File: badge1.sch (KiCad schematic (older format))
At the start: 21 parts, among them P1 CONN_01X04, P2 USB_A, P3 CONN_01X04, SW1 SW_PUSH, U1 badge_hole, U2 custom_logo, U3 Hillhacks_logo, U4 proto_area

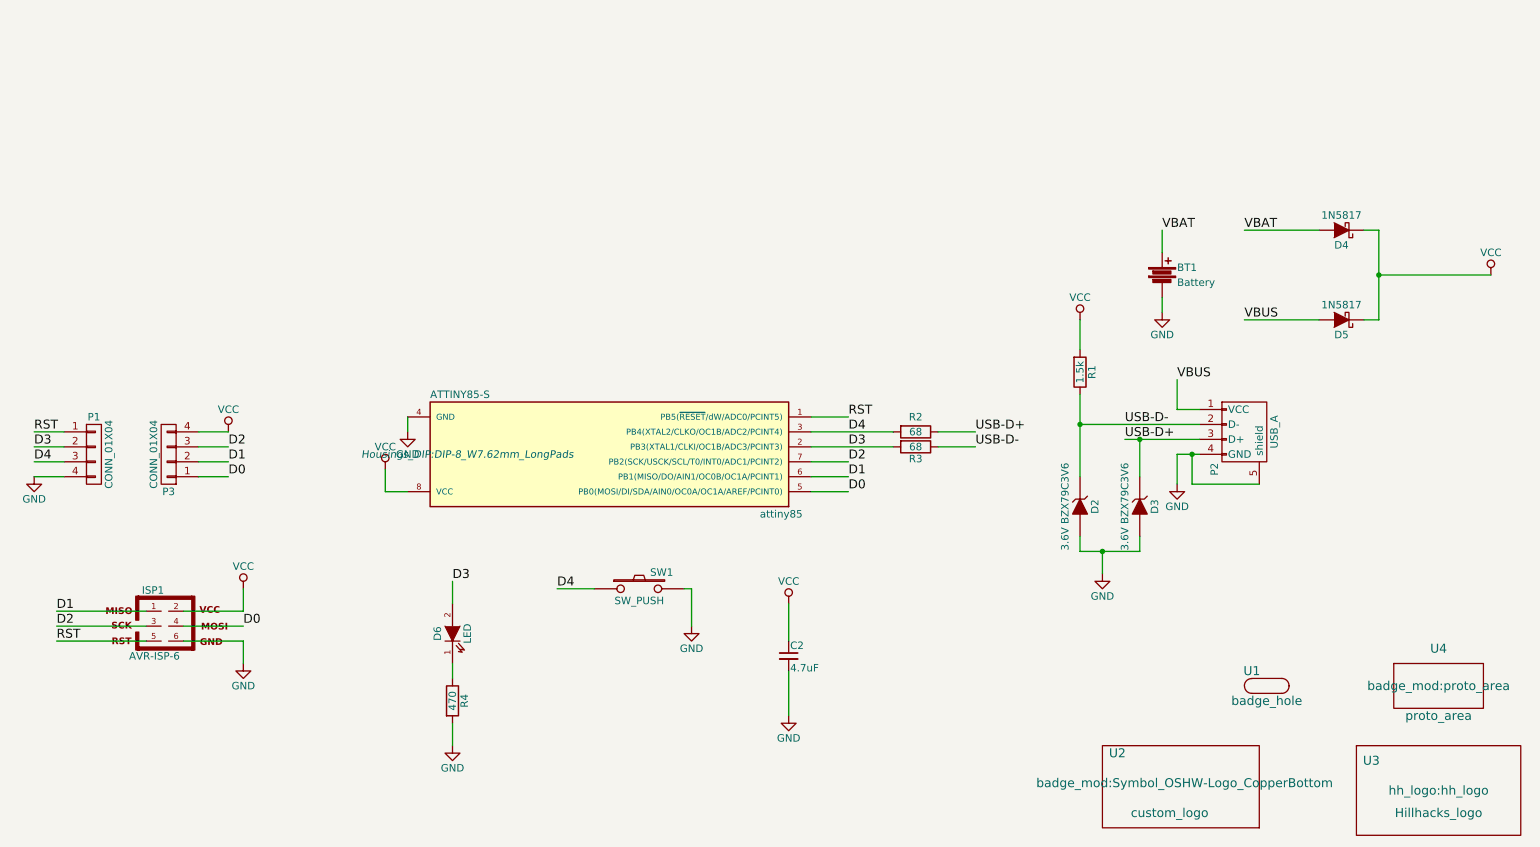
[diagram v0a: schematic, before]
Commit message: Updated with @anool's comments.
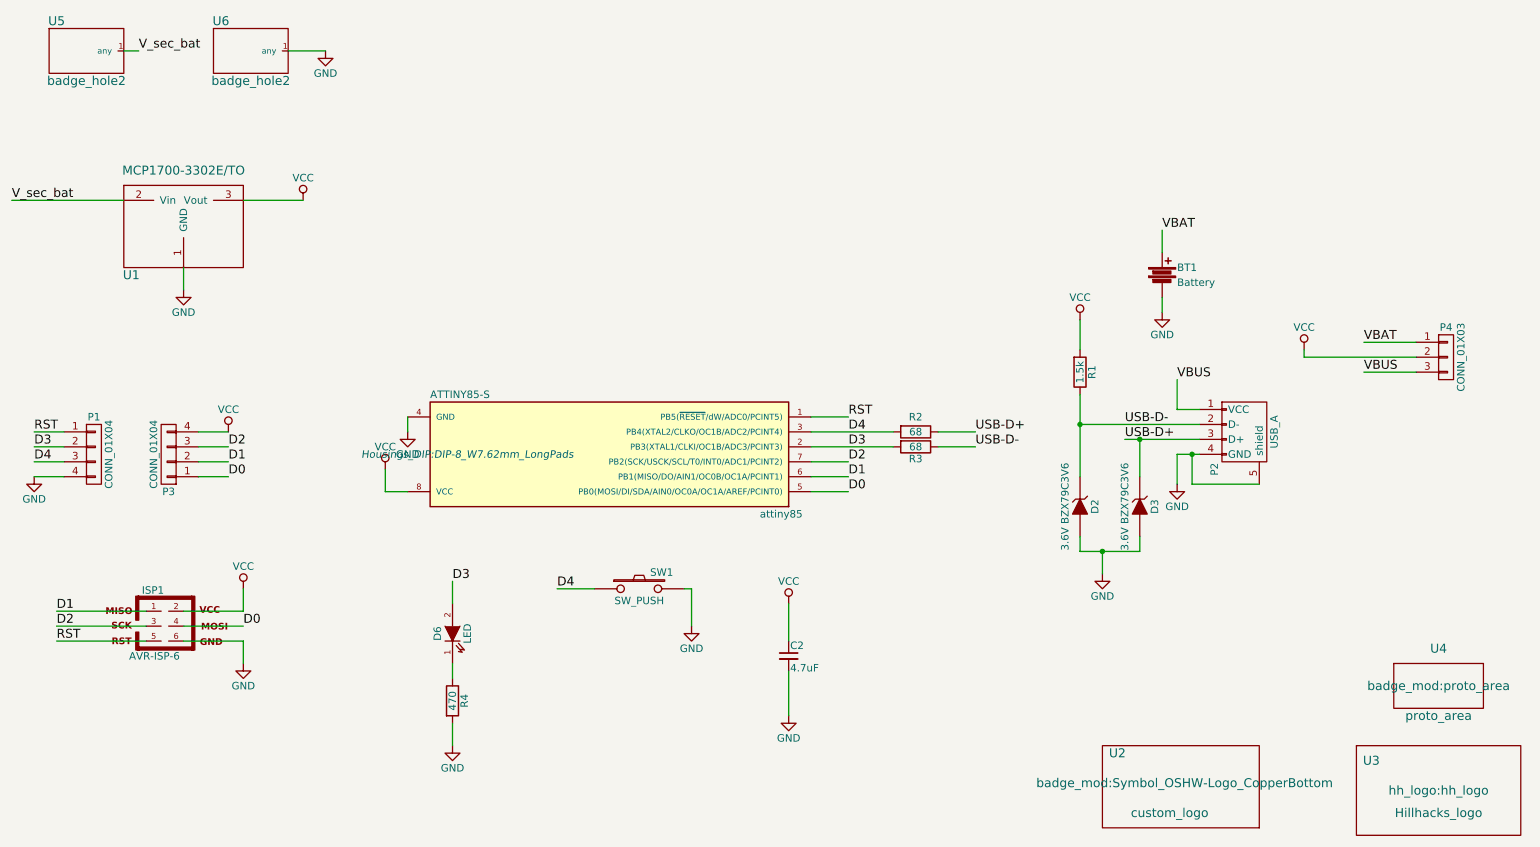
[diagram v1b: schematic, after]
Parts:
- removed D4, D5: 1N5817, Diodes_ThroughHole:Diode_DO-41_SOD81_Horizontal_RM10, symbol D_Schottky
- removed U1: badge_hole, badge_mod:badge_hole_6mmx3mm, symbol badge_hole
- added P4: CONN_01X03, Pin_Headers:Pin_Header_Straight_1x03, symbol CONN_01X03
- added U1: MCP1700-3302E/TO, TO_SOT_Packages_THT:TO-92_Molded_Narrow, symbol MCP1700-3302E/TO
- added U5, U6: badge_hole2, badge_mod:badge_hole_6mmx3mm(+2mmCu), symbol badge_hole2
- R1, R2, R3, R4: footprint Resistors_ThroughHole:Resistor_Vertical_RM5mm -> Resistors_ThroughHole:Resistor_Horizontal_RM10mm
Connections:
- net GND: now also U1.1 (GND), U6.1 (any)
- net VBAT: now also P4.1 (P1)
- net VBUS: now also P4.3 (P3)
- net VCC: now also P4.2 (P2), U1.3 (Vout)
- new net V_sec_bat: U1.2 (Vin), U5.1 (any)
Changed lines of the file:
@@
 RST
 $Comp
-L VCC #PWR01
+L VCC #PWR8
 U 1 1 56D1C9E6
 P 3350 3850
-F 0 "#PWR01" H 3350 3700 50  0001 C CNN
+F 0 "#PWR8" H 3350 3700 50  0001 C CNN
 F 1 "VCC" H 3350 4000 50  0000 C CNN
 F 2 "" H 3350 3850 50  0000 C CNN
@@
 $EndComp
 $Comp
-L GND #PWR02
+L GND #PWR9
 U 1 1 56D1CA06
 P 3500 3600
-F 0 "#PWR02" H 3500 3350 50  0001 C CNN
+F 0 "#PWR9" H 3500 3350 50  0001 C CNN
 F 1 "GND" H 3500 3450 50  0000 C CNN
 F 2 "" H 3500 3600 50  0000 C CNN
@@
 D0
 $Comp
-L GND #PWR03
+L GND #PWR17
 U 1 1 56D1CAE6
 P 8650 3950
-F 0 "#PWR03" H 8650 3700 50  0001 C CNN
+F 0 "#PWR17" H 8650 3700 50  0001 C CNN
 F 1 "GND" H 8650 3800 50  0000 C CNN
 F 2 "" H 8650 3950 50  0000 C CNN
@@
 F 0 "R3" V 6980 3700 50  0000 C CNN
 F 1 "68" V 6900 3700 50  0000 C CNN
-F 2 "Resistors_ThroughHole:Resistor_Vertical_RM5mm" V 6830 3700 50  0001 C CNN
+F 2 "Resistors_ThroughHole:Resistor_Horizontal_RM10mm" V 6830 3700 50  0001 C CNN
 F 3 "" H 6900 3700 50  0000 C CNN
 F 4 "311-68GRCT-ND" V 6900 3700 60  0001 C CNN "digikey"
@@
 F 0 "R2" V 6800 3600 50  0000 C CNN
 F 1 "68" V 6900 3600 50  0000 C CNN
-F 2 "Resistors_ThroughHole:Resistor_Vertical_RM5mm" V 6830 3600 50  0001 C CNN
+F 2 "Resistors_ThroughHole:Resistor_Horizontal_RM10mm" V 6830 3600 50  0001 C CNN
 F 3 "" H 6900 3600 50  0000 C CNN
 	1    6900 3600
@@
 $EndComp
 $Comp
-L GND #PWR04
+L GND #PWR15
 U 1 1 56D1CE23
 P 8150 4550
-F 0 "#PWR04" H 8150 4300 50  0001 C CNN
+F 0 "#PWR15" H 8150 4300 50  0001 C CNN
 F 1 "GND" H 8150 4400 50  0000 C CNN
 F 2 "" H 8150 4550 50  0000 C CNN
@@
 D0
 $Comp
-L GND #PWR05
+L GND #PWR5
 U 1 1 56D1D00C
 P 2400 5150
-F 0 "#PWR05" H 2400 4900 50  0001 C CNN
+F 0 "#PWR5" H 2400 4900 50  0001 C CNN
 F 1 "GND" H 2400 5000 50  0000 C CNN
 F 2 "" H 2400 5150 50  0000 C CNN
@@
 $EndComp
 $Comp
-L VCC #PWR06
+L VCC #PWR4
 U 1 1 56D1D050
 P 2400 4650
-F 0 "#PWR06" H 2400 4500 50  0001 C CNN
+F 0 "#PWR4" H 2400 4500 50  0001 C CNN
 F 1 "VCC" H 2400 4800 50  0000 C CNN
 F 2 "" H 2400 4650 50  0000 C CNN
@@
 $EndComp
 $Comp
-L GND #PWR07
+L GND #PWR13
 U 1 1 56D1D3A0
 P 6050 5500
-F 0 "#PWR07" H 6050 5250 50  0001 C CNN
+F 0 "#PWR13" H 6050 5250 50  0001 C CNN
 F 1 "GND" H 6050 5350 50  0000 C CNN
 F 2 "" H 6050 5500 50  0000 C CNN
@@
 $EndComp
 $Comp
-L VCC #PWR08
+L VCC #PWR12
 U 1 1 56D1D3F8
 P 6050 4750
-F 0 "#PWR08" H 6050 4600 50  0001 C CNN
+F 0 "#PWR12" H 6050 4600 50  0001 C CNN
 F 1 "VCC" H 6050 4900 50  0000 C CNN
 F 2 "" H 6050 4750 50  0000 C CNN
@@
 $EndComp
 $Comp
-L GND #PWR09
+L GND #PWR16
 U 1 1 56D1FCE5
 P 8550 2800
-F 0 "#PWR09" H 8550 2550 50  0001 C CNN
+F 0 "#PWR16" H 8550 2550 50  0001 C CNN
 F 1 "GND" H 8550 2650 50  0000 C CNN
 F 2 "" H 8550 2800 50  0000 C CNN
@@
 	0    1    1    0
 $EndComp
-$Comp
-L badge_hole U1
-U 1 1 56D21275
-P 9250 5300
-F 0 "U1" H 9150 5400 60  0000 C CNN
-F 1 "badge_hole" H 9250 5200 60  0000 C CNN
-F 2 "badge_mod:badge_hole_6mmx3mm" H 9250 5350 60  0001 C CNN
-F 3 "" H 9250 5350 60  0000 C CNN
-	1    9250 5300
-	1    0    0    -1
-$EndComp
 Text Label 8550 2250 0    60   ~ 0
 VBAT
 Text Label 8650 3250 0    60   ~ 0
 VBUS
-Text Label 9100 2250 0    60   ~ 0
+Text Label 9900 3000 0    60   ~ 0
 VBAT
-Text Label 9100 2850 0    60   ~ 0
+Text Label 9900 3200 0    60   ~ 0
 VBUS
 $Comp
@@
 $EndComp
 $Comp
-L GND #PWR010
+L GND #PWR10
 U 1 1 56D323D3
 P 3800 5700
-F 0 "#PWR010" H 3800 5450 50  0001 C CNN
+F 0 "#PWR10" H 3800 5450 50  0001 C CNN
 F 1 "GND" H 3800 5550 50  0000 C CNN
 F 2 "" H 3800 5700 50  0000 C CNN
@@
 F 0 "R4" V 3880 5400 50  0000 C CNN
 F 1 "470" V 3800 5400 50  0000 C CNN
-F 2 "Resistors_ThroughHole:Resistor_Vertical_RM5mm" V 3730 5400 50  0001 C CNN
+F 2 "Resistors_ThroughHole:Resistor_Horizontal_RM10mm" V 3730 5400 50  0001 C CNN
 F 3 "" H 3800 5400 50  0000 C CNN
 	1    3800 5400
@@
 D3
 $Comp
-L GND #PWR011
+L GND #PWR11
 U 1 1 56D3215E
 P 5400 4900
-F 0 "#PWR011" H 5400 4650 50  0001 C CNN
+F 0 "#PWR11" H 5400 4650 50  0001 C CNN
 F 1 "GND" H 5400 4750 50  0000 C CNN
 F 2 "" H 5400 4900 50  0000 C CNN
@@
 D4
 $Comp
-L GND #PWR012
+L GND #PWR1
 U 1 1 56D342D7
 P 1000 3900
-F 0 "#PWR012" H 1000 3650 50  0001 C CNN
+F 0 "#PWR1" H 1000 3650 50  0001 C CNN
 F 1 "GND" H 1000 3750 50  0000 C CNN
 F 2 "" H 1000 3900 50  0000 C CNN
@@
 D2
 $Comp
-L VCC #PWR013
+L VCC #PWR3
 U 1 1 56D3445E
 P 2300 3600
-F 0 "#PWR013" H 2300 3450 50  0001 C CNN
+F 0 "#PWR3" H 2300 3450 50  0001 C CNN
 F 1 "VCC" H 2300 3750 50  0000 C CNN
 F 2 "" H 2300 3600 50  0000 C CNN
@@
 $EndComp
 $Comp
-L VCC #PWR014
+L VCC #PWR18
 U 1 1 56D475E9
-P 10750 2550
-F 0 "#PWR014" H 10750 2400 50  0001 C CNN
-F 1 "VCC" H 10750 2700 50  0000 C CNN
-F 2 "" H 10750 2550 50  0000 C CNN
-F 3 "" H 10750 2550 50  0000 C CNN
-	1    10750 2550
+P 9500 3050
+F 0 "#PWR18" H 9500 2900 50  0001 C CNN
+F 1 "VCC" H 9500 3200 50  0000 C CNN
+F 2 "" H 9500 3050 50  0000 C CNN
+F 3 "" H 9500 3050 50  0000 C CNN
+	1    9500 3050
 	1    0    0    -1
 $EndComp
@@
 	1    10400 5300
 	1    0    0    -1
-$EndComp
-$Comp
-L D_Schottky D4
-U 1 1 56D72323
-P 9750 2250
-F 0 "D4" H 9750 2350 50  0000 C CNN
-F 1 " 1N5817" H 9750 2150 50  0000 C CNN
-F 2 "Diodes_ThroughHole:Diode_DO-41_SOD81_Horizontal_RM10" H 9750 2250 50  0001 C CNN
-F 3 "" H 9750 2250 50  0000 C CNN
-F 4 "1N5817DICT-ND " H 9750 2250 60  0001 C CNN "digikey"
-	1    9750 2250
-	-1   0    0    1
-$EndComp
-$Comp
-L D_Schottky D5
-U 1 1 56D72392
-P 9750 2850
-F 0 "D5" H 9750 2950 50  0000 C CNN
-F 1 "1N5817" H 9750 2750 50  0000 C CNN
-F 2 "Diodes_ThroughHole:Diode_DO-41_SOD81_Horizontal_RM10" H 9750 2850 50  0001 C CNN
-F 3 "" H 9750 2850 50  0000 C CNN
-F 4 "1N5817DICT-ND" H 9750 2850 60  0001 C CNN "digikey"
-	1    9750 2850
-	-1   0    0    1
 $EndComp
 $Comp
@@
 F 0 "R1" V 8080 3200 50  0000 C CNN
 F 1 "1.5k" V 8000 3200 50  0000 C CNN
-F 2 "Resistors_ThroughHole:Resistor_Vertical_RM5mm" V 7930 3200 50  0001 C CNN
+F 2 "Resistors_ThroughHole:Resistor_Horizontal_RM10mm" V 7930 3200 50  0001 C CNN
 F 3 "" H 8000 3200 50  0000 C CNN
 	1    8000 3200
@@
 $EndComp
 $Comp
-L VCC #PWR015
+L VCC #PWR14
 U 1 1 56D755A1
 P 8000 2850
-F 0 "#PWR015" H 8000 2700 50  0001 C CNN
+F 0 "#PWR14" H 8000 2700 50  0001 C CNN
 F 1 "VCC" H 8000 3000 50  0000 C CNN
 F 2 "" H 8000 2850 50  0000 C CNN
@@
 Wire Wire Line
 	8000 4400 8000 4300
-Connection ~ 10000 2550
-Wire Wire Line
-	10000 2250 9900 2250
-Wire Wire Line
-	10000 2250 10000 2850
-Wire Wire Line
-	10000 2850 9900 2850
 Wire Wire Line
 	2300 3900 2100 3900
@@
 	8550 2250 8550 2400
 Wire Wire Line
-	10000 2550 10750 2550
-Wire Wire Line
 	2300 3700 2100 3700
 Wire Wire Line
@@
 Wire Wire Line
 	3800 4600 3800 4750
-Wire Wire Line
-	9100 2850 9600 2850
-Wire Wire Line
-	9100 2250 9600 2250
 Connection ~ 8750 3750
 Wire Wire Line
@@
 Wire Wire Line
 	6450 3800 6200 3800
+$Comp
+L CONN_01X03 P4
+U 1 1 56D7F683
+P 10450 3100
+F 0 "P4" H 10450 3300 50  0000 C CNN
+F 1 "CONN_01X03" V 10550 3100 50  0000 C CNN
+F 2 "Pin_Headers:Pin_Header_Straight_1x03" H 10450 3100 50  0001 C CNN
+F 3 "" H 10450 3100 50  0000 C CNN
+	1    10450 3100
+	1    0    0    -1
+$EndComp
+Wire Wire Line
+	9900 3200 10250 3200
+Wire Wire Line
+	9900 3000 10250 3000
+Wire Wire Line
+	9500 3050 9500 3100
+Wire Wire Line
+	9500 3100 10250 3100
+$Comp
+L MCP1700-3302E/TO U1
+U 1 1 56D86D05
+P 2000 2200
+F 0 "U1" H 1650 1850 60  0000 C CNN
+F 1 "MCP1700-3302E/TO" H 2000 2550 60  0000 C CNN
+F 2 "TO_SOT_Packages_THT:TO-92_Molded_Narrow" H 2000 2000 60  0001 C CNN
+F 3 "" H 2000 2000 60  0000 C CNN
+	1    2000 2200
+	1    0    0    -1
+$EndComp
+$Comp
+L VCC #PWR6
+U 1 1 56D86F61
+P 2800 2050
+F 0 "#PWR6" H 2800 1900 50  0001 C CNN
+F 1 "VCC" H 2800 2200 50  0000 C CNN
+F 2 "" H 2800 2050 50  0000 C CNN
+F 3 "" H 2800 2050 50  0000 C CNN
+	1    2800 2050
+	1    0    0    -1
+$EndComp
+$Comp
+L GND #PWR2
+U 1 1 56D86FA3
+P 2000 2650
+F 0 "#PWR2" H 2000 2400 50  0001 C CNN
+F 1 "GND" H 2000 2500 50  0000 C CNN
+F 2 "" H 2000 2650 50  0000 C CNN
+F 3 "" H 2000 2650 50  0000 C CNN
+	1    2000 2650
+	1    0    0    -1
+$EndComp
+Text Label 850  2050 0    60   ~ 0
+V_sec_bat
+Wire Wire Line
+	850  2050 1600 2050
+Wire Wire Line
+	2400 2050 2800 2050
+Wire Wire Line
+	2000 2500 2000 2650
+Text Label 1700 1050 0    60   ~ 0
+V_sec_bat
+Wire Wire Line
+	1700 1050 1600 1050
+$Comp
+L GND #PWR7
+U 1 1 56D87B87
+P 2950 1050
+F 0 "#PWR7" H 2950 800 50  0001 C CNN
+F 1 "GND" H 2950 900 50  0000 C CNN
+F 2 "" H 2950 1050 50  0000 C CNN
+F 3 "" H 2950 1050 50  0000 C CNN
+	1    2950 1050
+	1    0    0    -1
+$EndComp
+Wire Wire Line
+	2950 1050 2700 1050
+$Comp
+L badge_hole2 U5
+U 1 1 56D88206
+P 1350 1050
+F 0 "U5" H 1150 1250 60  0000 C CNN
+F 1 "badge_hole2" H 1350 850 60  0000 C CNN
+F 2 "badge_mod:badge_hole_6mmx3mm(+2mmCu)" H 1350 1050 60  0001 C CNN
+F 3 "" H 1350 1050 60  0000 C CNN
+	1    1350 1050
+	1    0    0    -1
+$EndComp
+$Comp
+L badge_hole2 U6
+U 1 1 56D88276
+P 2450 1050
+F 0 "U6" H 2250 1250 60  0000 C CNN
+F 1 "badge_hole2" H 2450 850 60  0000 C CNN
+F 2 "badge_mod:badge_hole_6mmx3mm(+2mmCu)" H 2450 1050 60  0001 C CNN
+F 3 "" H 2450 1050 60  0000 C CNN
+	1    2450 1050
+	1    0    0    -1
+$EndComp
 $EndSCHEMATC

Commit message: added tessearact logo. smoothed 3 corners.
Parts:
- added U7: custom_logo, badge_mod:tesseract, symbol custom_logo
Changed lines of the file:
@@
 RST
 $Comp
-L VCC #PWR8
+L VCC #PWR01
 U 1 1 56D1C9E6
 P 3350 3850
-F 0 "#PWR8" H 3350 3700 50  0001 C CNN
+F 0 "#PWR01" H 3350 3700 50  0001 C CNN
 F 1 "VCC" H 3350 4000 50  0000 C CNN
 F 2 "" H 3350 3850 50  0000 C CNN
@@
 $EndComp
 $Comp
-L GND #PWR9
+L GND #PWR02
 U 1 1 56D1CA06
 P 3500 3600
-F 0 "#PWR9" H 3500 3350 50  0001 C CNN
+F 0 "#PWR02" H 3500 3350 50  0001 C CNN
 F 1 "GND" H 3500 3450 50  0000 C CNN
 F 2 "" H 3500 3600 50  0000 C CNN
@@
 D0
 $Comp
-L GND #PWR17
+L GND #PWR03
 U 1 1 56D1CAE6
 P 8650 3950
-F 0 "#PWR17" H 8650 3700 50  0001 C CNN
+F 0 "#PWR03" H 8650 3700 50  0001 C CNN
 F 1 "GND" H 8650 3800 50  0000 C CNN
 F 2 "" H 8650 3950 50  0000 C CNN
@@
 $EndComp
 $Comp
-L GND #PWR15
+L GND #PWR04
 U 1 1 56D1CE23
 P 8150 4550
-F 0 "#PWR15" H 8150 4300 50  0001 C CNN
+F 0 "#PWR04" H 8150 4300 50  0001 C CNN
 F 1 "GND" H 8150 4400 50  0000 C CNN
 F 2 "" H 8150 4550 50  0000 C CNN
@@
 D0
 $Comp
-L GND #PWR5
+L GND #PWR05
 U 1 1 56D1D00C
 P 2400 5150
-F 0 "#PWR5" H 2400 4900 50  0001 C CNN
+F 0 "#PWR05" H 2400 4900 50  0001 C CNN
 F 1 "GND" H 2400 5000 50  0000 C CNN
 F 2 "" H 2400 5150 50  0000 C CNN
@@
 $EndComp
 $Comp
-L VCC #PWR4
+L VCC #PWR06
 U 1 1 56D1D050
 P 2400 4650
-F 0 "#PWR4" H 2400 4500 50  0001 C CNN
+F 0 "#PWR06" H 2400 4500 50  0001 C CNN
 F 1 "VCC" H 2400 4800 50  0000 C CNN
 F 2 "" H 2400 4650 50  0000 C CNN
@@
 $EndComp
 $Comp
-L GND #PWR13
+L GND #PWR07
 U 1 1 56D1D3A0
 P 6050 5500
-F 0 "#PWR13" H 6050 5250 50  0001 C CNN
+F 0 "#PWR07" H 6050 5250 50  0001 C CNN
 F 1 "GND" H 6050 5350 50  0000 C CNN
 F 2 "" H 6050 5500 50  0000 C CNN
@@
 $EndComp
 $Comp
-L VCC #PWR12
+L VCC #PWR08
 U 1 1 56D1D3F8
 P 6050 4750
-F 0 "#PWR12" H 6050 4600 50  0001 C CNN
+F 0 "#PWR08" H 6050 4600 50  0001 C CNN
 F 1 "VCC" H 6050 4900 50  0000 C CNN
 F 2 "" H 6050 4750 50  0000 C CNN
@@
 $EndComp
 $Comp
-L GND #PWR16
+L GND #PWR09
 U 1 1 56D1FCE5
 P 8550 2800
-F 0 "#PWR16" H 8550 2550 50  0001 C CNN
+F 0 "#PWR09" H 8550 2550 50  0001 C CNN
 F 1 "GND" H 8550 2650 50  0000 C CNN
 F 2 "" H 8550 2800 50  0000 C CNN
@@
 $EndComp
 $Comp
-L GND #PWR10
+L GND #PWR010
 U 1 1 56D323D3
 P 3800 5700
-F 0 "#PWR10" H 3800 5450 50  0001 C CNN
+F 0 "#PWR010" H 3800 5450 50  0001 C CNN
 F 1 "GND" H 3800 5550 50  0000 C CNN
 F 2 "" H 3800 5700 50  0000 C CNN
@@
 D3
 $Comp
-L GND #PWR11
+L GND #PWR011
 U 1 1 56D3215E
 P 5400 4900
-F 0 "#PWR11" H 5400 4650 50  0001 C CNN
+F 0 "#PWR011" H 5400 4650 50  0001 C CNN
 F 1 "GND" H 5400 4750 50  0000 C CNN
 F 2 "" H 5400 4900 50  0000 C CNN
@@
 D4
 $Comp
-L GND #PWR1
+L GND #PWR012
 U 1 1 56D342D7
 P 1000 3900
-F 0 "#PWR1" H 1000 3650 50  0001 C CNN
+F 0 "#PWR012" H 1000 3650 50  0001 C CNN
 F 1 "GND" H 1000 3750 50  0000 C CNN
 F 2 "" H 1000 3900 50  0000 C CNN
@@
 D2
 $Comp
-L VCC #PWR3
+L VCC #PWR013
 U 1 1 56D3445E
 P 2300 3600
-F 0 "#PWR3" H 2300 3450 50  0001 C CNN
+F 0 "#PWR013" H 2300 3450 50  0001 C CNN
 F 1 "VCC" H 2300 3750 50  0000 C CNN
 F 2 "" H 2300 3600 50  0000 C CNN
@@
 $EndComp
 $Comp
-L VCC #PWR18
+L VCC #PWR014
 U 1 1 56D475E9
 P 9500 3050
-F 0 "#PWR18" H 9500 2900 50  0001 C CNN
+F 0 "#PWR014" H 9500 2900 50  0001 C CNN
 F 1 "VCC" H 9500 3200 50  0000 C CNN
 F 2 "" H 9500 3050 50  0000 C CNN
@@
 $EndComp
 $Comp
-L VCC #PWR14
+L VCC #PWR015
 U 1 1 56D755A1
 P 8000 2850
-F 0 "#PWR14" H 8000 2700 50  0001 C CNN
+F 0 "#PWR015" H 8000 2700 50  0001 C CNN
 F 1 "VCC" H 8000 3000 50  0000 C CNN
 F 2 "" H 8000 2850 50  0000 C CNN
@@
 $EndComp
 $Comp
-L VCC #PWR6
+L VCC #PWR016
 U 1 1 56D86F61
 P 2800 2050
-F 0 "#PWR6" H 2800 1900 50  0001 C CNN
+F 0 "#PWR016" H 2800 1900 50  0001 C CNN
 F 1 "VCC" H 2800 2200 50  0000 C CNN
 F 2 "" H 2800 2050 50  0000 C CNN
@@
 $EndComp
 $Comp
-L GND #PWR2
+L GND #PWR017
 U 1 1 56D86FA3
 P 2000 2650
-F 0 "#PWR2" H 2000 2400 50  0001 C CNN
+F 0 "#PWR017" H 2000 2400 50  0001 C CNN
 F 1 "GND" H 2000 2500 50  0000 C CNN
 F 2 "" H 2000 2650 50  0000 C CNN
@@
 	1700 1050 1600 1050
 $Comp
-L GND #PWR7
+L GND #PWR018
 U 1 1 56D87B87
 P 2950 1050
-F 0 "#PWR7" H 2950 800 50  0001 C CNN
+F 0 "#PWR018" H 2950 800 50  0001 C CNN
 F 1 "GND" H 2950 900 50  0000 C CNN
 F 2 "" H 2950 1050 50  0000 C CNN
@@
 	1    0    0    -1
 $EndComp
+$Comp
+L custom_logo U7
+U 1 1 56E01DAC
+P 8650 5200
+F 0 "U7" H 8200 5400 60  0000 C CNN
+F 1 "custom_logo" H 8550 5000 60  0000 C CNN
+F 2 "badge_mod:tesseract" H 8650 5200 60  0000 C CNN
+F 3 "" H 8650 5200 60  0000 C CNN
+	1    8650 5200
+	1    0    0    -1
+$EndComp

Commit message: minor changes. increase via size. update rendering with colour.
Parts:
- SW1: footprint Buttons_Switches_ThroughHole:SW_TH_Tactile_Omron_B3F-10xx -> badge_mod:OPL_DIP_BUTTON_TS-1109_BEST_SHENZEN
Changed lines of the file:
@@
 F 0 "SW1" H 5200 4760 50  0000 C CNN
 F 1 "SW_PUSH" H 5050 4570 50  0000 C CNN
-F 2 "Buttons_Switches_ThroughHole:SW_TH_Tactile_Omron_B3F-10xx" H 5050 4650 50  0001 C CNN
+F 2 "badge_mod:OPL_DIP_BUTTON_TS-1109_BEST_SHENZEN" H 5050 4650 50  0001 C CNN
 F 3 "" H 5050 4650 50  0000 C CNN
 	1    5050 4650
